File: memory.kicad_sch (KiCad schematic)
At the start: 19 parts, among them U2 IS43TR16640C-125JBL

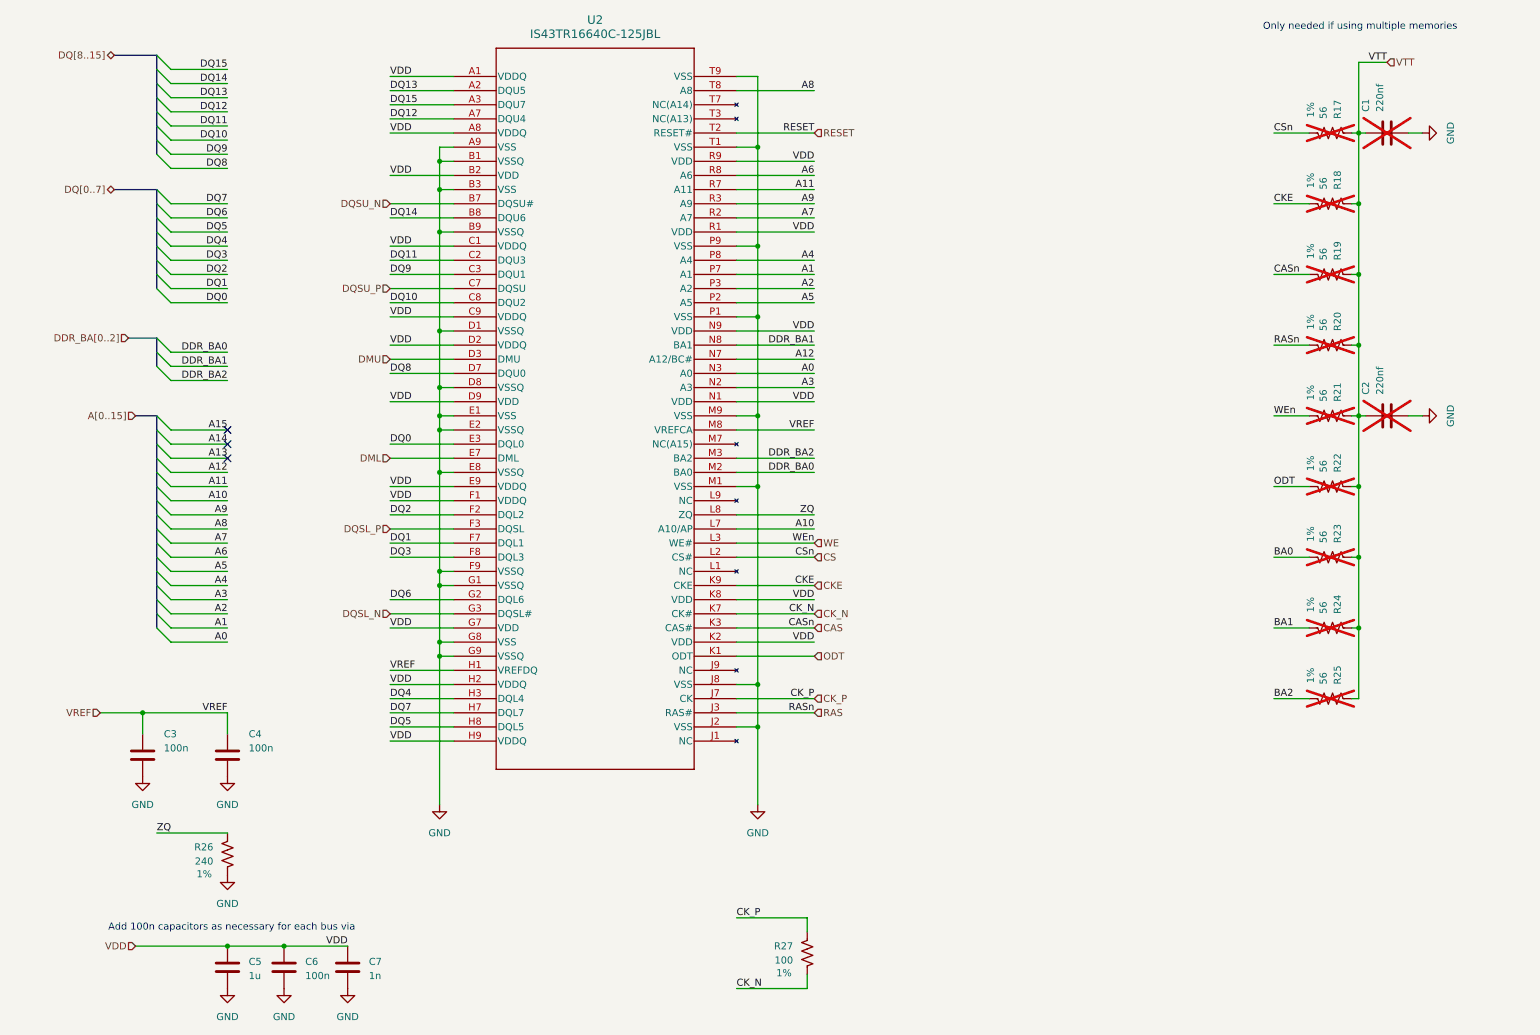
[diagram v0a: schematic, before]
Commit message: Progress on DDR routing
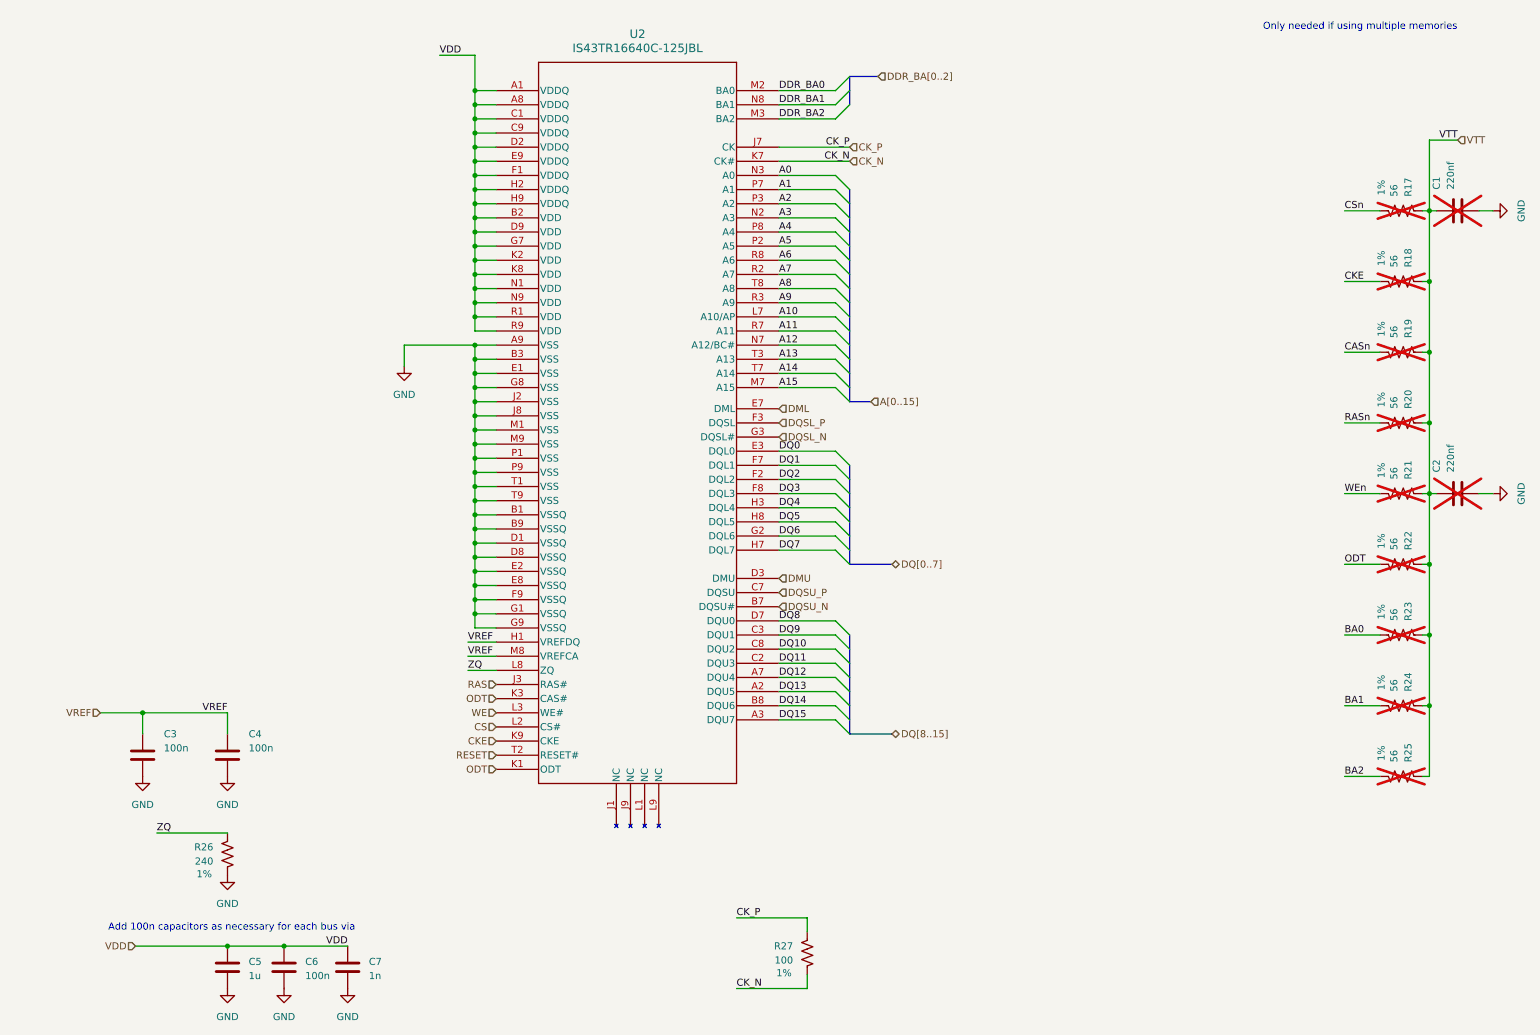
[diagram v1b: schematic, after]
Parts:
- U2: footprint footprints:TW-BGA96L_9X13X1.2_ISI -> TW-BGA96L_9X13X1.2_ISI
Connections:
- net A13: now also U2.T3 (A13)
- net A14: now also U2.T7 (A14)
- net A15: now also U2.M7 (A15)
- net CS: no longer R17.2
- net ODT: now also U2.K3 (CAS#)
- net RAS: no longer R20.2
- net WE: no longer R21.2
- net CAS renamed CASn
- net CASn: no longer U2.K3 (CAS#)
- new net CSn: R17.2
- new net RASn: R20.2
- new net WEn: R21.2
- no-connect marks 3 -> 0
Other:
- moved on the sheet: C1, C2, R17, R18, R19, R20, R21, R22, R23, R24, R25

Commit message: Routing routing routing
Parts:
- added C80, C81, C82, C83, C84, C85, C86, C87, C88: 3.3nF, Capacitor_SMD:C_0402_1005Metric, symbol SparkFun-Capacitor:C
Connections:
- net DQ0: now also U2.F2 (DQL2); no longer U2.E3 (DQL0)
- net DQ1: now also U2.G2 (DQL6); no longer U2.F7 (DQL1)
- net DQ10: now also U2.A7 (DQU4); no longer U2.C8 (DQU2)
- net DQ11: now also U2.D7 (DQU0); no longer U2.C2 (DQU3)
- net DQ12: now also U2.A2 (DQU5); no longer U2.A7 (DQU4)
- net DQ13: now also U2.C3 (DQU1); no longer U2.A2 (DQU5)
- net DQ14: now also U2.C2 (DQU3); no longer U2.B8 (DQU6)
- net DQ15: now also U2.C8 (DQU2); no longer U2.A3 (DQU7)
- net DQ2: now also U2.H3 (DQL4); no longer U2.F2 (DQL2)
- net DQ3: now also U2.E3 (DQL0); no longer U2.F8 (DQL3)
- net DQ4: now also U2.H8 (DQL5); no longer U2.H3 (DQL4)
- net DQ5: now also U2.F8 (DQL3); no longer U2.H8 (DQL5)
- net DQ6: now also U2.F7 (DQL1); no longer U2.G2 (DQL6)
- net DQ8: now also U2.B8 (DQU6); no longer U2.D7 (DQU0)
- net DQ9: now also U2.A3 (DQU7); no longer U2.C3 (DQU1)
- net GND: now also C80.2, C81.2, C82.2, C83.2, C84.2, C85.2, C86.2, C87.2, C88.2
- net ODT: no longer U2.K3 (CAS#)
- net VDD: now also C80.1, C81.1, C82.1, C83.1, C84.1, C85.1, C86.1, C87.1, C88.1
- new net CAS: U2.K3 (CAS#)

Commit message: eMMC routing done
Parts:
- U2: footprint TW-BGA96L_9X13X1.2_ISI -> footprints:TW-BGA96L_9X13X1.2_ISI
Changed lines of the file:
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@@
 			)
 		)
-		(property "Footprint" "TW-BGA96L_9X13X1.2_ISI"
+		(property "Footprint" "footprints:TW-BGA96L_9X13X1.2_ISI"
 			(at 97.282 23.876 0)
 			(effects

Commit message: WIP
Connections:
- net DQ1: now also U2.F7 (DQL1); no longer U2.G2 (DQL6)
- net DQ11: now also U2.A3 (DQU7); no longer U2.D7 (DQU0)
- net DQ13: now also U2.B8 (DQU6); no longer U2.C3 (DQU1)
- net DQ14: now also U2.C8 (DQU2); no longer U2.C2 (DQU3)
- net DQ15: now also U2.C2 (DQU3); no longer U2.C8 (DQU2)
- net DQ4: now also U2.H7 (DQL7); no longer U2.H8 (DQL5)
- net DQ5: now also U2.H8 (DQL5); no longer U2.F8 (DQL3)
- net DQ6: now also U2.F8 (DQL3); no longer U2.F7 (DQL1)
- net DQ7: now also U2.G2 (DQL6); no longer U2.H7 (DQL7)
- net DQ8: now also U2.D7 (DQU0); no longer U2.B8 (DQU6)
- net DQ9: now also U2.C3 (DQU1); no longer U2.A3 (DQU7)

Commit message: progress
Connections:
- net DQ0: now also U2.H3 (DQL4); no longer U2.F2 (DQL2)
- net DQ1: now also U2.G2 (DQL6); no longer U2.F7 (DQL1)
- net DQ10: now also U2.D7 (DQU0); no longer U2.A7 (DQU4)
- net DQ13: now also U2.C3 (DQU1); no longer U2.B8 (DQU6)
- net DQ14: now also U2.B8 (DQU6); no longer U2.C8 (DQU2)
- net DQ15: now also U2.A7 (DQU4); no longer U2.C2 (DQU3)
- net DQ2: now also U2.H7 (DQL7); no longer U2.H3 (DQL4)
- net DQ3: now also U2.F2 (DQL2); no longer U2.E3 (DQL0)
- net DQ4: now also U2.F8 (DQL3); no longer U2.H7 (DQL7)
- net DQ5: now also U2.F7 (DQL1); no longer U2.H8 (DQL5)
- net DQ6: now also U2.H8 (DQL5); no longer U2.F8 (DQL3)
- net DQ7: now also U2.E3 (DQL0); no longer U2.G2 (DQL6)
- net DQ8: now also U2.C2 (DQU3); no longer U2.D7 (DQU0)
- net DQ9: now also U2.C8 (DQU2); no longer U2.C3 (DQU1)
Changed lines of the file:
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@@
 		)
 	)
-	(label "DQ10"
+	(label "DQ15"
 		(at 149.86 135.89 0)
 		(fields_autoplaced yes)
@@
 		)
 	)
-	(label "DQ13"
+	(label "DQ14"
 		(at 149.86 140.97 0)
-		(effects
-			(font
-				(size 1.27 1.27)
-			)
-			(justify left bottom)
-		)
-	)
-	(label "DQ6"
+		(fields_autoplaced yes)
+		(effects
+			(font
+				(size 1.27 1.27)
+			)
+			(justify left bottom)
+		)
+	)
+	(label "DQ4"
 		(at 149.86 102.87 0)
+		(fields_autoplaced yes)
 		(effects
 			(font
@@
 		)
 	)
-	(label "DQ5"
+	(label "DQ6"
 		(at 149.86 107.95 0)
+		(fields_autoplaced yes)
 		(effects
 			(font
@@
 		)
 	)
-	(label "DQ4"
+	(label "DQ2"
 		(at 149.86 113.03 0)
+		(fields_autoplaced yes)
 		(effects
 			(font
@@
 	(label "DQ11"
 		(at 149.86 143.51 0)
+		(fields_autoplaced yes)
 		(effects
 			(font
@@
 		)
 	)
-	(label "DQ3"
+	(label "DQ7"
 		(at 149.86 95.25 0)
+		(fields_autoplaced yes)
 		(effects
 			(font
@@
 		)
 	)
-	(label "DQ0"
+	(label "DQ3"
 		(at 149.86 100.33 0)
+		(fields_autoplaced yes)
+		(effects
+			(font
+				(size 1.27 1.27)
+			)
+			(justify left bottom)
+		)
+	)
+	(label "DQ10"
+		(at 149.86 125.73 0)
+		(fields_autoplaced yes)
 		(effects
 			(font
@@
 	)
 	(label "DQ8"
-		(at 149.86 125.73 0)
-		(effects
-			(font
-				(size 1.27 1.27)
-			)
-			(justify left bottom)
-		)
-	)
-	(label "DQ15"
 		(at 149.86 133.35 0)
+		(fields_autoplaced yes)
 		(effects
 			(font
@@
 		)
 	)
-	(label "DQ7"
+	(label "DQ1"
 		(at 149.86 110.49 0)
+		(fields_autoplaced yes)
 		(effects
 			(font
@@
 		)
 	)
-	(label "DQ1"
+	(label "DQ5"
 		(at 149.86 97.79 0)
+		(fields_autoplaced yes)
 		(effects
 			(font
@@
 		)
 	)
-	(label "DQ14"
+	(label "DQ9"
 		(at 149.86 130.81 0)
+		(fields_autoplaced yes)
 		(effects
 			(font
@@
 		)
 	)
-	(label "DQ2"
+	(label "DQ0"
 		(at 149.86 105.41 0)
+		(fields_autoplaced yes)
 		(effects
 			(font
@@
 		)
 	)
-	(label "DQ9"
+	(label "DQ13"
 		(at 149.86 128.27 0)
-		(effects
-			(font
+		(fields_autoplaced yes)
+		(effects
+			(font

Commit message: DDR added switch backs
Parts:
- C7, C80, C81, C82, C83, C84, C85, C86, C87, C88: footprint Capacitor_SMD:C_0402_1005Metric -> Capacitor_SMD:C_0201_0603Metric
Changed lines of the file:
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@@
 			)
 		)
-		(property "Footprint" "Capacitor_SMD:C_0402_1005Metric"
+		(property "Footprint" "Capacitor_SMD:C_0201_0603Metric"
 			(at 17.4752 55.88 0)
 			(effects
@@
 			)
 		)
-		(property "Footprint" "Capacitor_SMD:C_0402_1005Metric"
+		(property "Footprint" "Capacitor_SMD:C_0201_0603Metric"
 			(at 39.0652 39.37 0)
 			(effects
@@
 			)
 		)
-		(property "Footprint" "Capacitor_SMD:C_0402_1005Metric"
+		(property "Footprint" "Capacitor_SMD:C_0201_0603Metric"
 			(at 67.0052 39.37 0)
 			(effects
@@
 			)
 		)
-		(property "Footprint" "Capacitor_SMD:C_0402_1005Metric"
+		(property "Footprint" "Capacitor_SMD:C_0201_0603Metric"
 			(at 53.0352 39.37 0)
 			(effects
@@
 			)
 		)
-		(property "Footprint" "Capacitor_SMD:C_0402_1005Metric"
+		(property "Footprint" "Capacitor_SMD:C_0201_0603Metric"
 			(at 59.3852 55.88 0)
 			(effects
@@
 			)
 		)
-		(property "Footprint" "Capacitor_SMD:C_0402_1005Metric"
+		(property "Footprint" "Capacitor_SMD:C_0201_0603Metric"
 			(at 73.3552 55.88 0)
 			(effects
@@
 			)
 		)
-		(property "Footprint" "Capacitor_SMD:C_0402_1005Metric"
+		(property "Footprint" "Capacitor_SMD:C_0201_0603Metric"
 			(at 73.3552 199.39 0)
 			(effects
@@
 			)
 		)
-		(property "Footprint" "Capacitor_SMD:C_0402_1005Metric"
+		(property "Footprint" "Capacitor_SMD:C_0201_0603Metric"
 			(at 25.0952 39.37 0)
 			(effects
@@
 			)
 		)
-		(property "Footprint" "Capacitor_SMD:C_0402_1005Metric"
+		(property "Footprint" "Capacitor_SMD:C_0201_0603Metric"
 			(at 45.4152 55.88 0)
 			(effects
@@
 			)
 		)
-		(property "Footprint" "Capacitor_SMD:C_0402_1005Metric"
+		(property "Footprint" "Capacitor_SMD:C_0201_0603Metric"
 			(at 31.4452 55.88 0)
 			(effects

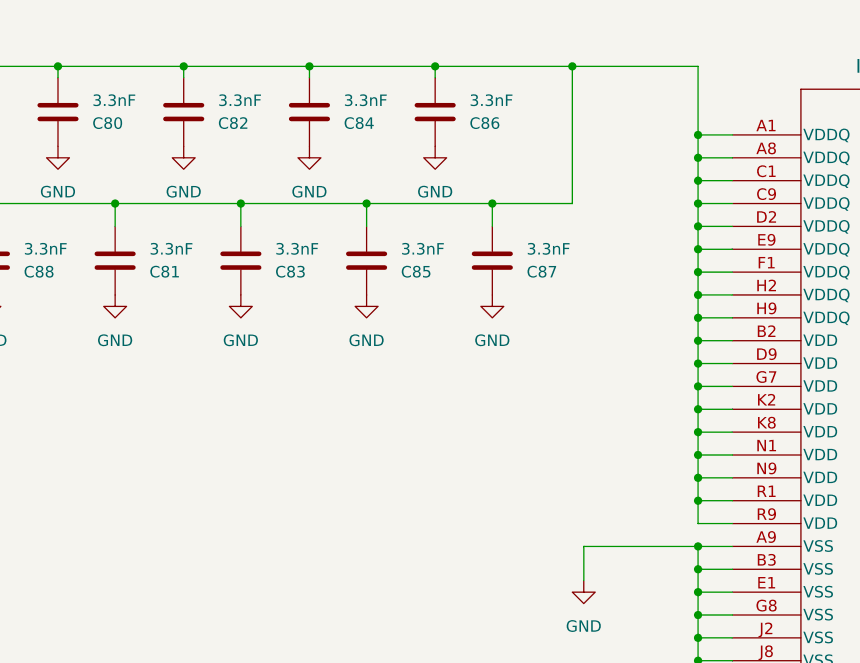
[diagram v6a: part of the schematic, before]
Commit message: DDR added switch backs cont
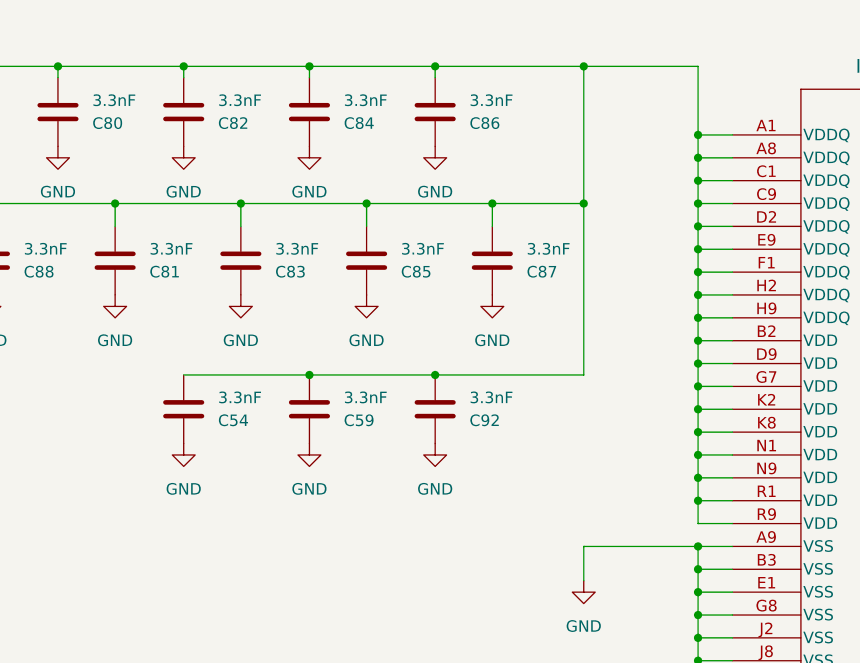
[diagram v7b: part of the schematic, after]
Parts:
- added C54, C59, C92: 3.3nF, Capacitor_SMD:C_0201_0603Metric, symbol SparkFun-Capacitor:C
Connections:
- net GND: now also C54.2, C59.2, C92.2
- net VDD: now also C54.1, C59.1, C92.1

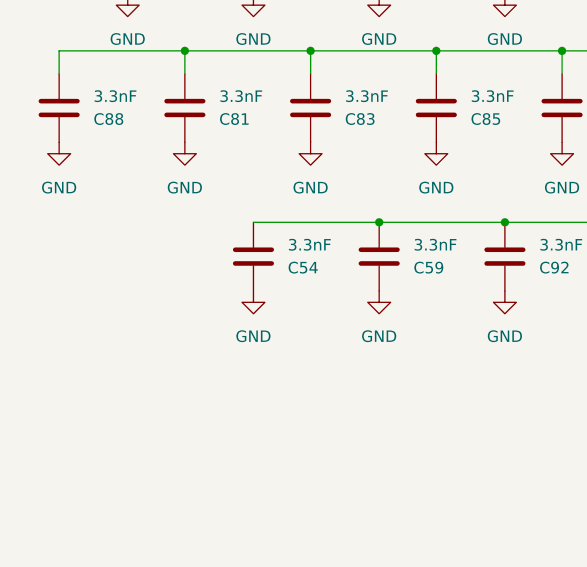
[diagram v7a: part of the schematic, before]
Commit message: More DDR Routing
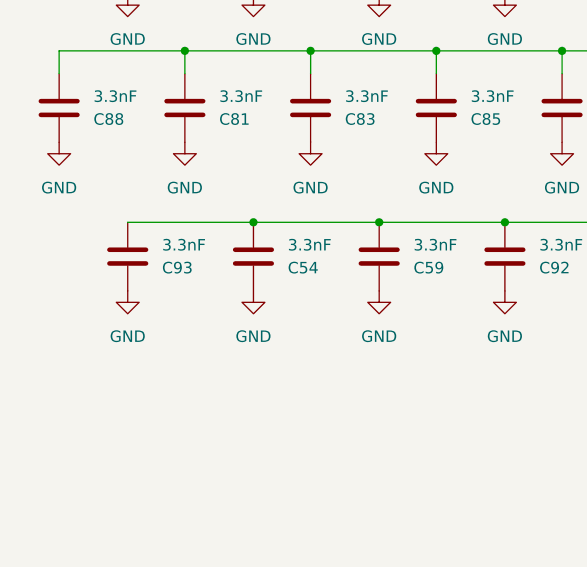
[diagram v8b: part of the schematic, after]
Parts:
- added C93: 3.3nF, Capacitor_SMD:C_0201_0603Metric, symbol SparkFun-Capacitor:C
- C3, C4: footprint Capacitor_SMD:C_0402_1005Metric -> Capacitor_SMD:C_0201_0603Metric
- R26: footprint Resistor_SMD:R_0402_1005Metric -> Resistor_SMD:R_0201_0603Metric
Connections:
- net GND: now also C93.2
- net VDD: now also C93.1
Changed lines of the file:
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@@
 	)
 	(junction
+		(at 38.1 57.15)
+		(diameter 0)
+		(color 0 0 0 0)
+	)
+	(junction
 		(at 95.25 119.38)
 		(diameter 0)
@@
 		)
 	)
+	(wire
+		(pts
+			(xy 24.13 57.15) (xy 38.1 57.15)
+		)
+		(stroke
+			(width 0)
+			(type default)
+		)
+	)
 	(bus
 		(pts
@@
 			)
 		)
-		(property "Footprint" "Capacitor_SMD:C_0402_1005Metric"
+		(property "Footprint" "Capacitor_SMD:C_0201_0603Metric"
 			(at 36.5252 161.29 0)
 			(effects
@@
 			)
 		)
-		(property "Footprint" "Resistor_SMD:R_0402_1005Metric"
+		(property "Footprint" "Resistor_SMD:R_0201_0603Metric"
 			(at 46.228 167.64 0)
 			(effects
@@
 	)
 	(symbol
+		(lib_id "power:GND")
+		(at 24.13 64.77 0)
+		(unit 1)
+		(exclude_from_sim no)
+		(in_bom yes)
+		(on_board yes)
+		(dnp no)
+		(fields_autoplaced yes)
+		(property "Reference" "#PWR0257"
+			(at 24.13 71.12 0)
+			(effects
+				(font
+					(size 1.27 1.27)
+				)
+				(hide yes)
+			)
+		)
+		(property "Value" "GND"
+			(at 24.13 69.85 0)
+			(effects
+				(font
+					(size 1.27 1.27)
+				)
+			)
+		)
+		(property "Footprint" ""
+			(at 24.13 64.77 0)
+			(effects
+				(font
+					(size 1.27 1.27)
+				)
+				(hide yes)
+			)
+		)
+		(property "Datasheet" ""
+			(at 24.13 64.77 0)
+			(effects
+				(font
+					(size 1.27 1.27)
+				)
+				(hide yes)
+			)
+		)
+		(property "Description" "Power symbol creates a global label with name \"GND\" , ground"
+			(at 24.13 64.77 0)
+			(effects
+				(font
+					(size 1.27 1.27)
+				)
+				(hide yes)
+			)
+		)
+		(pin "1"
+		)
+		(instances
+			(project "SBC"
+				(path "/21bb932a-ec67-4661-9215-0551f718d1c0/1a39d522-2eb7-49c0-a4cb-6db909b7fe44"
+					(reference "#PWR0257")
+					(unit 1)
+				)
+			)
+		)
+	)
+	(symbol
 		(lib_id "SparkFun-Capacitor:C")
 		(at 72.39 44.45 0)
@@
 	(symbol
 		(lib_id "SparkFun-Capacitor:C")
+		(at 24.13 60.96 0)
+		(unit 1)
+		(exclude_from_sim no)
+		(in_bom yes)
+		(on_board yes)
+		(dnp no)
+		(property "Reference" "C93"
+			(at 27.94 62.23 0)
+			(effects
+				(font
+					(size 1.27 1.27)
+				)
+				(justify left)
+			)
+		)
+		(property "Value" "3.3nF"
+			(at 27.94 59.6899 0)
+			(effects
+				(font
+					(size 1.27 1.27)
+				)
+				(justify left)
+			)
+		)
+		(property "Footprint" "Capacitor_SMD:C_0201_0603Metric"
+			(at 25.0952 72.39 0)
+			(effects
+				(font
+					(size 1.27 1.27)
+				)
+				(hide yes)
+			)
+		)
+		(property "Datasheet" ""
+			(at 25.4 77.47 0)
+			(effects
+				(font
+					(size 1.27 1.27)
+				)
+				(hide yes)
+			)
+		)
+		(property "Description" ""
+			(at 30.734 64.77 0)
+			(effects
+				(font
+					(size 1.27 1.27)
+				)
+			)
+		)
+		(property "PROD_ID" ""
+			(at 24.13 74.93 0)
+			(effects
+				(font
+					(size 1.27 1.27)
+				)
+			)
+		)
+		(property "Voltage" ""
+			(at 27.94 62.2299 0)
+			(effects
+				(font
+					(size 1.27 1.27)
+				)
+				(justify left)
+			)
+		)
+		(pin "1"
+		)
+		(pin "2"
+		)
+		(instances
+			(project "SBC"
+				(path "/21bb932a-ec67-4661-9215-0551f718d1c0/1a39d522-2eb7-49c0-a4cb-6db909b7fe44"
+					(reference "C93")
+					(unit 1)
+				)
+			)
+		)
+	)
+	(symbol
+		(lib_id "SparkFun-Capacitor:C")
 		(at 30.48 44.45 0)
 		(unit 1)
@@
 			)
 		)
-		(property "Footprint" "Capacitor_SMD:C_0402_1005Metric"
+		(property "Footprint" "Capacitor_SMD:C_0201_0603Metric"
 			(at 51.7652 161.29 0)
 			(effects
